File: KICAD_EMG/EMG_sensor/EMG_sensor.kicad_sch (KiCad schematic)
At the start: 42 parts, among them J1 Conn_01x03_Pin, J2 Conn_01x01_Pin, J3 Conn_01x01_Pin, J4 Conn_01x01_Pin, J5 Conn_01x02_Pin, U1 TL081, U2 TL081, U3 TL081, U4 TL081, U5 TL081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

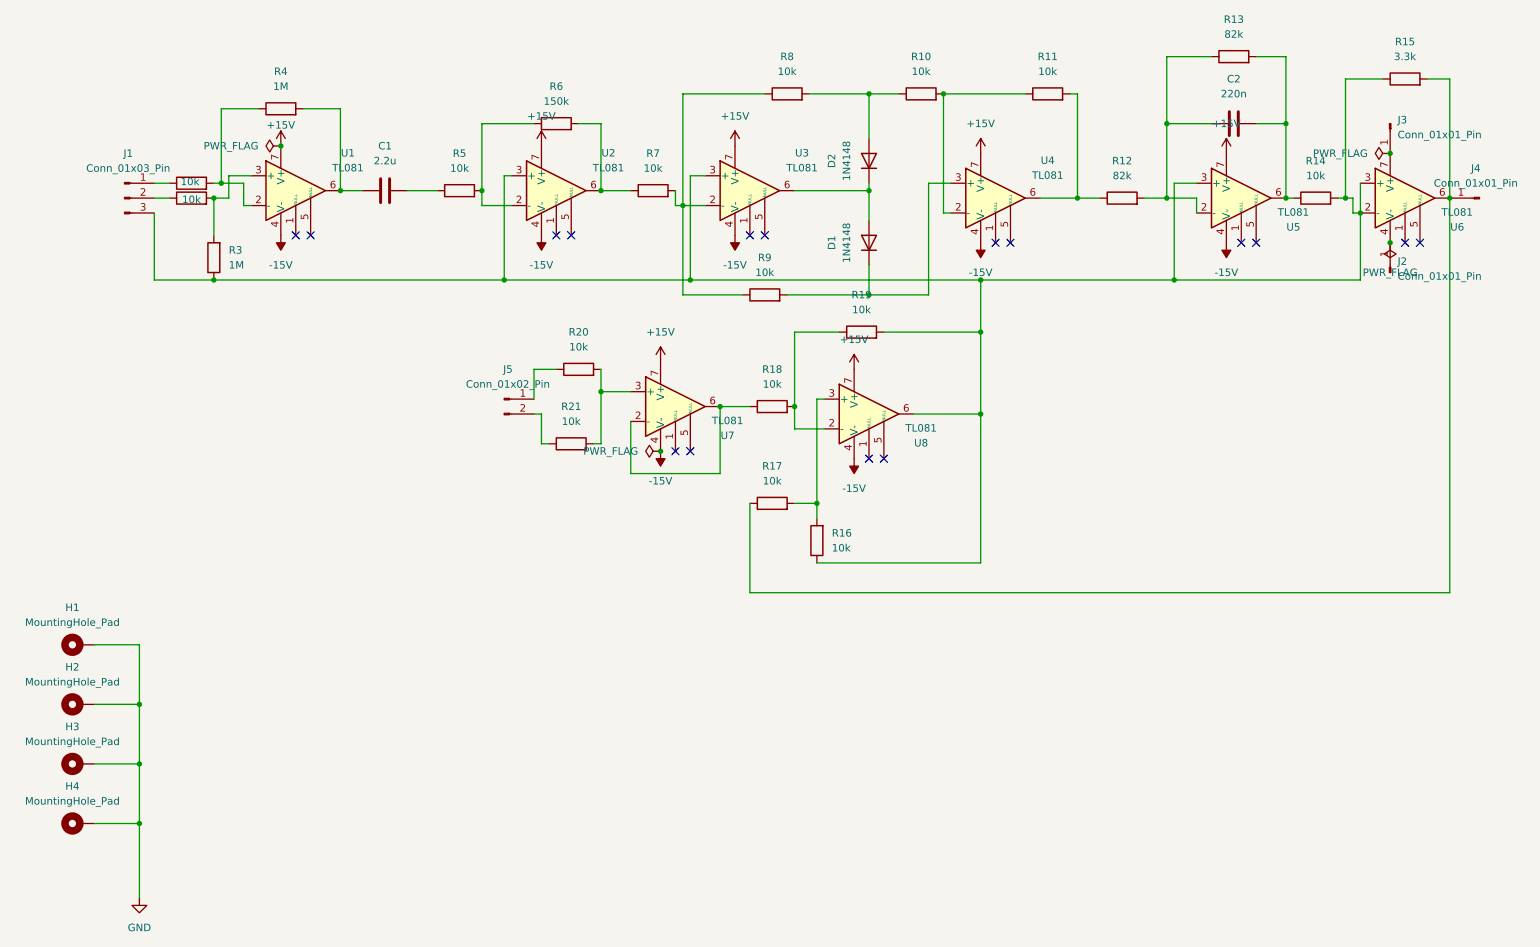
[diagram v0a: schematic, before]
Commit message: le PCB avec les piste à 0.3 et 0 erreur
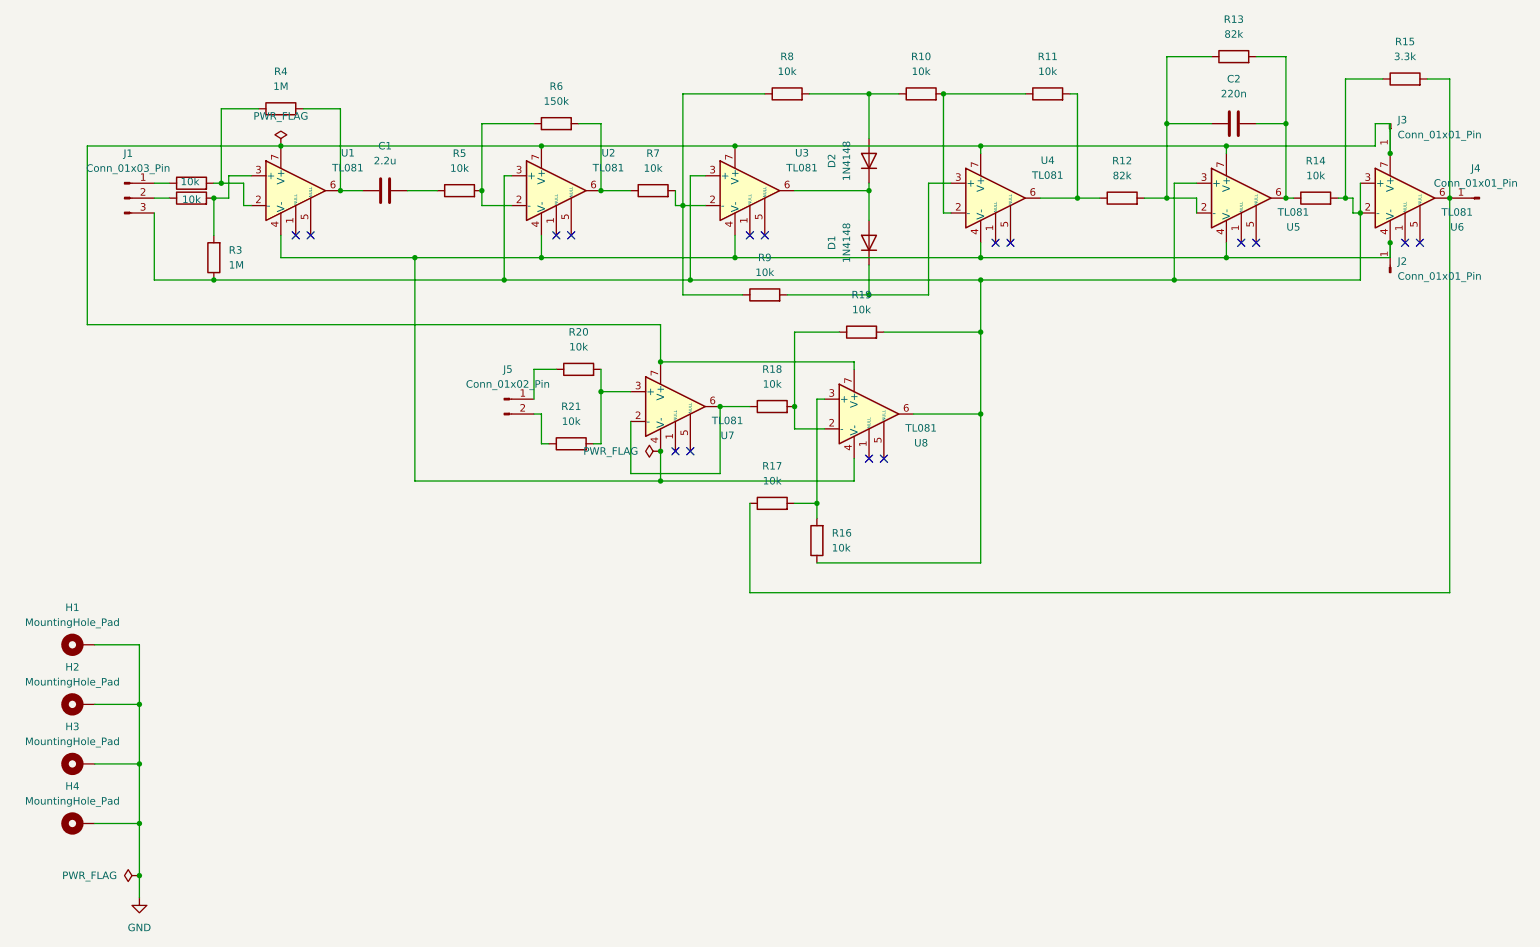
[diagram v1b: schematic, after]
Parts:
- C1, C2: footprint Capacitor_SMD:C_0201_0603Metric_Pad0.64x0.40mm_HandSolder -> Capacitor_SMD:C_0402_1005Metric_Pad0.74x0.62mm_HandSolder
- D1, D2: footprint Diode_SMD:D_0201_0603Metric_Pad0.64x0.40mm_HandSolder -> Diode_SMD:D_SOD-123
- R1, R10, R11, R12, R13, R14, R15, R16, R17, R18, R19, R2, R20, R21, R3, R4, R5, R6, R7, R8, R9: footprint Resistor_SMD:R_0201_0603Metric_Pad0.64x0.40mm_HandSolder -> Resistor_SMD:R_0402_1005Metric_Pad0.72x0.64mm_HandSolder
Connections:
- net +15V is gone; now on an unnamed net: U1.7 (V+), U2.7 (V+), U3.7 (V+), U4.7 (V+), U5.7 (V+), U7.7 (V+), U8.7 (V+)
- net -15V is gone; now on an unnamed net: U1.4 (V-), U2.4 (V-), U3.4 (V-), U4.4 (V-), U5.4 (V-), U7.4 (V-), U8.4 (V-)
